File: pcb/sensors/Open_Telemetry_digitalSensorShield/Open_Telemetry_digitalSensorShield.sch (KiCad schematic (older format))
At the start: 37 parts, among them IC1 L80-M39, J1 73412-0110, J2 Conn_01x12_Female, J3 Conn_01x16_Female, Q1 BC846BPN, U1 BME280, U2 MPU-9250

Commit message: 2'nd internal review
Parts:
- removed R11, R12, R13, R14, R15, R16, R17: 1k, RESC0603X26N, symbol RC0201JR-071KL:RC0201JR-071KL
- removed R2: 10k, RESC0603X26N, symbol RC0201JR-0710KL:RC0201JR-0710KL
- added R10, R11, R12, R13: 62, Open_Telemetry:RESC1005X40N, symbol RC0402JR-0762RL:RC0402JR-0762RL
- added R14: 130, Open_Telemetry:RESC1005X40N, symbol CRCW0402130RJNED:CRCW0402130RJNED
- added R15, R16: 10k, Open_Telemetry:RESC0603X26N, symbol RC0201JR-0710KL:RC0201JR-0710KL
- C1, C2, C3, C4: footprint CAPC1608X87N -> Open_Telemetry:CAPC1608X87N
- C5: footprint CAPC1005X55N -> Open_Telemetry:CAPC1005X55N
- IC1: footprint L80-M39 -> Open_Telemetry:L80-M39
- J1: value 73412-0110 -> Ext GPS antenna connector
- J2: value Conn_01x12_Female -> PinHeader_01x12
- J3: value Conn_01x16_Female -> PinHeader_01x16
- LED1: value ExtAnt -> EXT ANT
- LED3: renamed from D1; value ASMB-MTB1-0A3A2 -> System Status
- R1: footprint RESC0603X26N -> Open_Telemetry:RESC0603X26N
- R2: renamed from R3; footprint RESC0603X26N -> Open_Telemetry:RESC0603X26N
- R3: renamed from R4; footprint RESC0603X26N -> Open_Telemetry:RESC0603X26N
- R5: renamed from R6; footprint RESC0603X26N -> Open_Telemetry:RESC0603X26N
- R6: renamed from R7; footprint RESC0603X26N -> Open_Telemetry:RESC0603X26N
- R9: renamed from R10; footprint RESC0603X26N -> Open_Telemetry:RESC0603X26N
- renumbered R5 to R4, R8 to R7, R9 to R8
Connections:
- net +3V3: now also U1.2 (CSB), R15.1, R16.1
- net BLUE_LED: now also R12.1
- net CALIB: now also R16.2
- net EXT_ANT: now also R10.1
- net GND: now also R4.1, S1.2, S2.2; no longer R4.2
- net GREEN_LED: now also R13.1
- net RED_LED: now also R14.1
- net RESET: now also R15.2
- net SAT_LOCK: now also R11.1
- net UART_1_CLIENT_RXD: now also J3.8 (Pin_8); no longer J3.9 (Pin_9)
- net UART_1_CLIENT_TXD: now also J3.9 (Pin_9); no longer J3.10 (Pin_10)
- net at R1.2, U1.5 (SDO): now also R4.2; no longer R4.1
- net at LED3.1 (RK): now also R14.2
- net at LED3.2 (GK): now also R13.2
- net at LED3.3 (BK): now also R12.2
- net at LED1.2 (A): now also R10.2
- net at LED2.2 (A): now also R11.2
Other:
- note added: "50 Ohm impedience strip\nto optional active external\nGPS antenna\nKeep short - 50 Ohms\n@1.54 GHz center Freq."
- note added: "9 Axis Accel- + Gyro- + Magnetometer"
- note added: "Buttons & indications"
- note added: "ESP32 Huzzah feather HAT/SHIELD Connections"
- note added: "I2C communication only. Listening to I2C_0 non real time bus,\nI2C address: 0x77 (default) or 0x76 if optioal R5 is mounted."
- note added: "I2C communication only. Listening to I2C_1 real time bus,\nI2C address: 0x68 (default) or 0x69 if optioal R8 is mounted."
- note removed: "50 Ohm impedience strip"
- note removed: "9 axis accel- + gyro- + magnetometer"
- note removed: "Buttons & lights"
- note removed: "ESP32 HAT/SHIELD CONNECTIONS"
- note removed: "I2C communication only. Listening to I2C_0 non real time bus,\nI2C address: 0x77 (default) or 0x76 if optioal Rxx is mounted."
- note removed: "I2C communication only. Listening to I2C_1 real time bus,\nI2C address: 0x68 (default) or 0x69 if optioal Rxx is mounted."
- moved on the sheet: C1, C3, C4, C5, C6, C7, C8, J2, LED1, LED2, LED3, R1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

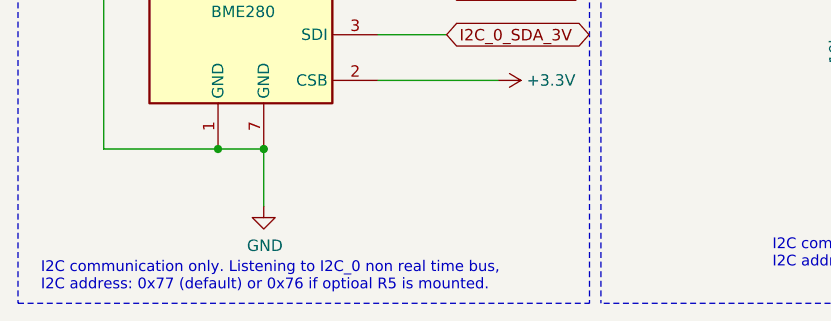
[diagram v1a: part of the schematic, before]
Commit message: OFT001v1 Inertial HW board ready for internal review. Find it underpcb/sensors/Open_Telemetry_digitalSensorShield/...
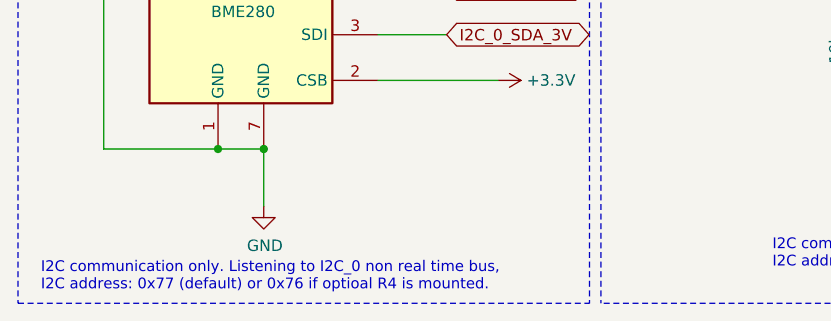
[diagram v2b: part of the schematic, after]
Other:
- note added: "I2C communication only. Listening to I2C_0 non real time bus,\nI2C address: 0x77 (default) or 0x76 if optioal R4 is mounted."
- note removed: "I2C communication only. Listening to I2C_0 non real time bus,\nI2C address: 0x77 (default) or 0x76 if optioal R5 is mounted."
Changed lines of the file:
@@
 $EndComp
 Text Notes 750  7050 0    47   ~ 0
-I2C communication only. Listening to I2C_0 non real time bus,\nI2C address: 0x77 (default) or 0x76 if optioal R5 is mounted.
+I2C communication only. Listening to I2C_0 non real time bus,\nI2C address: 0x77 (default) or 0x76 if optioal R4 is mounted.
 $Comp
 L power:GND #PWR011

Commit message: First candidate for prototype manufacturing of OFT001 P1A01 sent to PCBWay after a early feedback. Close to manufacturing goahead.
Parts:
- removed S1: RST, Open_Telemetry:ATS2D1G, symbol ATS2D1G_NC_LFS:ATS2D1G_NC_LFS
- removed S2: CALIB, Open_Telemetry:ATS2D1G, symbol ATS2D1G_NC_LFS:ATS2D1G_NC_LFS
- added S1: RST, Open_Telemetry:KSR, symbol KSR223GLFG:KSR223GLFG
- added S2: CALIB, Open_Telemetry:KSR, symbol KSR223GLFG:KSR223GLFG
- R8: footprint RESC0603X26N -> Open_Telemetry:RESC0603X26N
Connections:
- net CALIB: now also S2.1
- net GND: now also S1.2, S2.2
- net RESET: now also S1.1
- no-connect marks 0 -> 17
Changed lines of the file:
@@
 Sheet 1 1
 Title "OFT001v1"
-Date "2019-11-12"
-Rev "P0A.03"
+Date "2019-11-17"
+Rev "P1A_01 Prot. manf."
 Comp "OpenFly Telemetry"
 Comment1 "© 2019 - Jonas Bjurel"
@@
 F 0 "R8" H 4600 5750 50  0000 L CNN
 F 1 "10k" H 4575 5575 50  0000 L CNN
-F 2 "RESC0603X26N" H 4850 5700 50  0001 L CNN
+F 2 "Open_Telemetry:RESC0603X26N" H 4850 5700 50  0001 L CNN
 F 3 "http://www.yageo.com/documents/recent/PYu-RC0201_51_RoHS_L_8.pdf" H 4850 5600 50  0001 L CNN
 F 4 "THICK FILM CHIP RESISTORS" H 4850 5500 50  0001 L CNN "Description"
@@
 Text GLabel 10050 2400 1    50   BiDi ~ 0
 RESET
-Wire Wire Line
-	10750 4000 10750 4050
 $Comp
 L LED:ASMB-MTB1-0A3A2 LED3
@@
 	0    1    1    0
 $EndComp
-$Comp
-L ATS2D1G_NC_LFS:ATS2D1G_NC_LFS S1
-U 1 1 5DC11E0D
-P 10050 3200
-F 0 "S1" H 10400 3350 50  0000 L CNN
-F 1 "RST" H 10375 3075 50  0000 L CNN
-F 2 "Open_Telemetry:ATS2D1G" H 10700 3300 50  0001 L CNN
-F 3 "http://www.mouser.com/ds/2/60/ats-1100738.pdf" H 10700 3200 50  0001 L CNN
-F 4 "Tactile Switches 1VA 32VDC 50mA On-(On) Sldr IP54" H 10700 3100 50  0001 L CNN "Description"
-F 5 "" H 10700 3000 50  0001 L CNN "Height"
-F 6 "C & K COMPONENTS" H 10700 2900 50  0001 L CNN "Manufacturer_Name"
-F 7 "ATS2D1G NC LFS" H 10700 2800 50  0001 L CNN "Manufacturer_Part_Number"
-F 8 "611-ATS2D1GNCLFS" H 10700 2700 50  0001 L CNN "Mouser Part Number"
-F 9 "https://www.mouser.com/Search/Refine.aspx?Keyword=611-ATS2D1GNCLFS" H 10700 2600 50  0001 L CNN "Mouser Price/Stock"
-F 10 "" H 10700 2500 50  0001 L CNN "RS Part Number"
-F 11 "" H 10700 2400 50  0001 L CNN "RS Price/Stock"
-	1    10050 3200
-	0    1    1    0
-$EndComp
-$Comp
-L ATS2D1G_NC_LFS:ATS2D1G_NC_LFS S2
-U 1 1 5DC296C0
-P 10750 3200
-F 0 "S2" H 11100 3350 50  0000 L CNN
-F 1 "CALIB" H 11050 3075 50  0000 L CNN
-F 2 "Open_Telemetry:ATS2D1G" H 11400 3300 50  0001 L CNN
-F 3 "http://www.mouser.com/ds/2/60/ats-1100738.pdf" H 11400 3200 50  0001 L CNN
-F 4 "Tactile Switches 1VA 32VDC 50mA On-(On) Sldr IP54" H 11400 3100 50  0001 L CNN "Description"
-F 5 "" H 11400 3000 50  0001 L CNN "Height"
-F 6 "C & K COMPONENTS" H 11400 2900 50  0001 L CNN "Manufacturer_Name"
-F 7 "ATS2D1G NC LFS" H 11400 2800 50  0001 L CNN "Manufacturer_Part_Number"
-F 8 "611-ATS2D1GNCLFS" H 11400 2700 50  0001 L CNN "Mouser Part Number"
-F 9 "https://www.mouser.com/Search/Refine.aspx?Keyword=611-ATS2D1GNCLFS" H 11400 2600 50  0001 L CNN "Mouser Price/Stock"
-F 10 "" H 11400 2500 50  0001 L CNN "RS Part Number"
-F 11 "" H 11400 2400 50  0001 L CNN "RS Price/Stock"
-	1    10750 3200
-	0    1    1    0
-$EndComp
 Wire Wire Line
 	5400 4400 5400 4550
@@
 Wire Wire Line
 	10450 3200 10750 3200
-Connection ~ 10750 3200
 Wire Wire Line
 	8250 2550 8250 2725
@@
 	8250 3425 8250 3450
 Wire Wire Line
-	7650 2500 7650 2725
-Wire Wire Line
 	7650 3425 7650 3450
 Wire Wire Line
@@
 Wire Wire Line
 	9750 3175 10050 3175
-Connection ~ 10050 3175
-Wire Wire Line
-	10050 3175 10050 3200
 Wire Wire Line
 	9750 2400 9750 2325
 Wire Wire Line
-	10000 5950 9150 5950
-Wire Wire Line
 	9150 5950 9150 6200
 $Comp
@@
 	1    0    0    -1
 $EndComp
+NoConn ~ 10000 5050
+NoConn ~ 10000 5150
+NoConn ~ 10000 5250
+NoConn ~ 10000 5650
+NoConn ~ 10000 5750
+NoConn ~ 8150 5400
+NoConn ~ 8150 5500
+NoConn ~ 8150 5600
+NoConn ~ 8150 5700
+NoConn ~ 8150 5000
+NoConn ~ 8150 4900
+NoConn ~ 8150 4800
+NoConn ~ 6000 5350
+NoConn ~ 6000 5450
+NoConn ~ 4150 1350
+NoConn ~ 10000 6050
+NoConn ~ 10000 5850
+$Comp
+L power:PWR_FLAG #FLG0101
+U 1 1 5DD84330
+P 10650 5850
+F 0 "#FLG0101" H 10650 5925 50  0001 C CNN
+F 1 "PWR_FLAG" H 10650 6023 50  0000 C CNN
+F 2 "" H 10650 5850 50  0001 C CNN
+F 3 "~" H 10650 5850 50  0001 C CNN
+	1    10650 5850
+	1    0    0    -1
+$EndComp
+$Comp
+L power:GND #PWR0104
+U 1 1 5DD8DA9A
+P 10650 5850
+F 0 "#PWR0104" H 10650 5600 50  0001 C CNN
+F 1 "GND" H 10655 5677 50  0000 C CNN
+F 2 "" H 10650 5850 50  0001 C CNN
+F 3 "" H 10650 5850 50  0001 C CNN
+	1    10650 5850
+	1    0    0    -1
+$EndComp
 Wire Wire Line
-	10050 4000 10050 4075
+	9150 5950 10000 5950
+$Comp
+L power:PWR_FLAG #FLG0102
+U 1 1 5DD98FE2
+P 10650 5275
+F 0 "#FLG0102" H 10650 5350 50  0001 C CNN
+F 1 "PWR_FLAG" H 10650 5448 50  0000 C CNN
+F 2 "" H 10650 5275 50  0001 C CNN
+F 3 "~" H 10650 5275 50  0001 C CNN
+	1    10650 5275
+	-1   0    0    1
+$EndComp
+$Comp
+L power:+3.3V #PWR0105
+U 1 1 5DD99E4C
+P 10650 5275
+F 0 "#PWR0105" H 10650 5125 50  0001 C CNN
+F 1 "+3.3V" H 10665 5448 50  0000 C CNN
+F 2 "" H 10650 5275 50  0001 C CNN
+F 3 "" H 10650 5275 50  0001 C CNN
+	1    10650 5275
+	1    0    0    -1
+$EndComp
+Wire Wire Line
+	7650 2500 7650 2725
+$Comp
+L KSR223GLFG:KSR223GLFG S1
+U 1 1 5DE37D90
+P 10050 3300
+F 0 "S1" H 10300 3175 50  0000 L CNN
+F 1 "RST" H 10275 3475 50  0000 L CNN
+F 2 "Open_Telemetry:KSR" H 10350 3100 50  0001 C CNN
+F 3 "https://www.ckswitches.com/media/1466/ksr.pdf" H 10350 3000 50  0001 C CNN
+F 4 "Subminiature Tact Switch for SMT" H 10350 2900 50  0001 C CNN "Description"
+F 5 "" H 10350 2800 50  0001 C CNN "Height"
+F 6 "C & K COMPONENTS" H 10350 2700 50  0001 C CNN "Manufacturer_Name"
+F 7 "KSR223GLFG" H 10350 2600 50  0001 C CNN "Manufacturer_Part_Number"
+F 8 "611-KSR223GLFG" H 10350 2500 50  0001 C CNN "Mouser Part Number"
+F 9 "https://www.mouser.com/Search/Refine.aspx?Keyword=611-KSR223GLFG" H 10350 2400 50  0001 C CNN "Mouser Price/Stock"
+F 10 "" H 10350 2300 50  0001 C CNN "RS Part Number"
+F 11 "" H 10350 2200 50  0001 C CNN "RS Price/Stock"
+	1    10050 3300
+	0    1    1    0
+$EndComp
+Wire Wire Line
+	10050 3900 10050 4075
+Wire Wire Line
+	10050 3175 10050 3300
+Connection ~ 10050 3175
+$Comp
+L KSR223GLFG:KSR223GLFG S2
+U 1 1 5DE74ED7
+P 10750 3300
+F 0 "S2" H 11000 3175 50  0000 L CNN
+F 1 "CALIB" H 10975 3475 50  0000 L CNN
+F 2 "Open_Telemetry:KSR" H 11050 3100 50  0001 C CNN
+F 3 "https://www.ckswitches.com/media/1466/ksr.pdf" H 11050 3000 50  0001 C CNN
+F 4 "Subminiature Tact Switch for SMT" H 11050 2900 50  0001 C CNN "Description"
+F 5 "" H 11050 2800 50  0001 C CNN "Height"
+F 6 "C & K COMPONENTS" H 11050 2700 50  0001 C CNN "Manufacturer_Name"
+F 7 "KSR223GLFG" H 11050 2600 50  0001 C CNN "Manufacturer_Part_Number"
+F 8 "611-KSR223GLFG" H 11050 2500 50  0001 C CNN "Mouser Part Number"
+F 9 "https://www.mouser.com/Search/Refine.aspx?Keyword=611-KSR223GLFG" H 11050 2400 50  0001 C CNN "Mouser Price/Stock"
+F 10 "" H 11050 2300 50  0001 C CNN "RS Part Number"
+F 11 "" H 11050 2200 50  0001 C CNN "RS Price/Stock"
+	1    10750 3300
+	0    1    1    0
+$EndComp
+Wire Wire Line
+	10750 3900 10750 4050
+Wire Wire Line
+	10750 3300 10750 3200
+Connection ~ 10750 3200
 $EndSCHEMATC

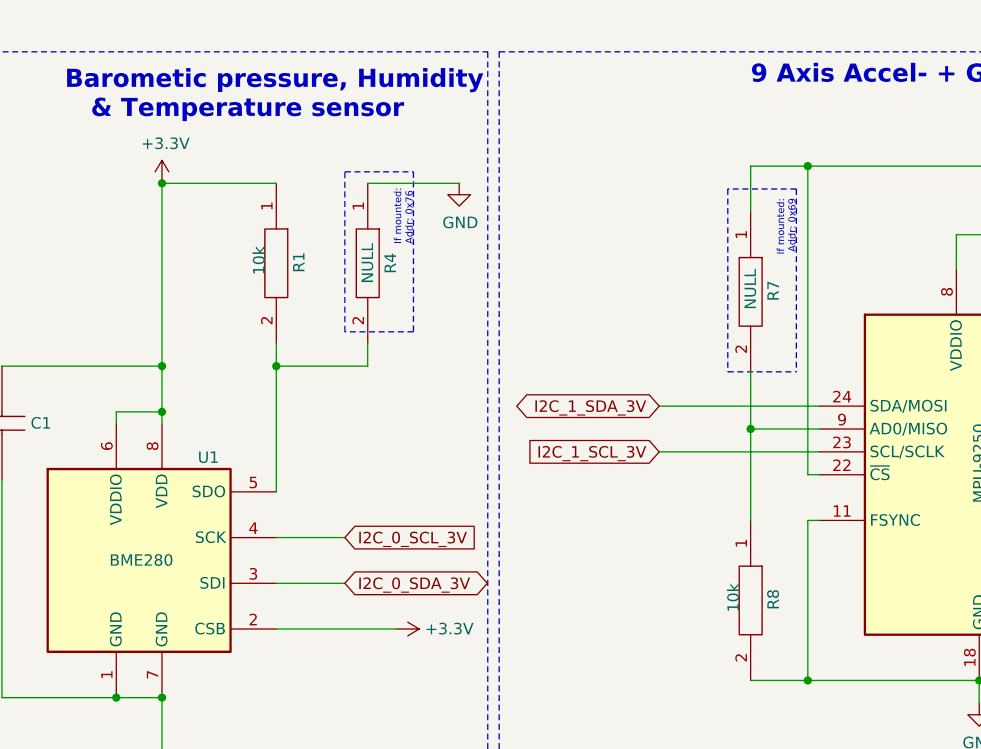
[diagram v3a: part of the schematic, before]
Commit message: P1A02 files sent to manufactuing review. Added R17, R18, R19, RR20 I2C pullups for reliability and hiher speeds.
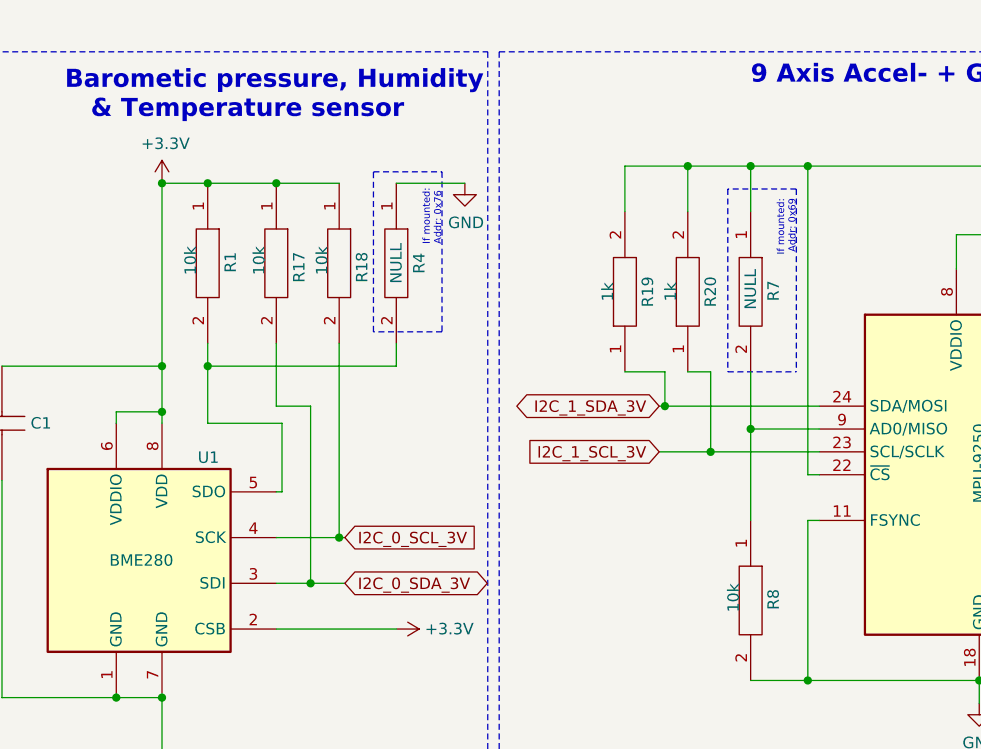
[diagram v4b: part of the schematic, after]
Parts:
- added R17, R18: 10k, Open_Telemetry:RESC0603X26N, symbol RC0201JR-0710KL:RC0201JR-0710KL
- added R19, R20: 1k, Open_Telemetry:RESC0603X26N, symbol RC0201JR-071KL:RC0201JR-071KL
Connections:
- net +3V3: now also R17.1, R18.1, R19.2, R20.2
- net I2C_0_SCL_3V: now also R18.2
- net I2C_0_SDA_3V: now also R17.2
- net I2C_1_SCL_3V: now also R20.1
- net I2C_1_SDA_3V: now also R19.1
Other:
- moved on the sheet: R1, R4

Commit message: Corrected the error where BME280 was placed as U1 instead of BMP280 This is the baseline that will be delivered as the P1A prototype card.
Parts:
- U1: value BME280 -> BMP280; symbol Sensor:BME280 -> Sensor_Pressure:BMP280
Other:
- moved on the sheet: C1, U1
